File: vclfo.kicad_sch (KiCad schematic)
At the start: 39 parts, among them U10 tl072, U11 tl072, U6 tl072, U7 lm13700, U8 tl072, U9 tl072

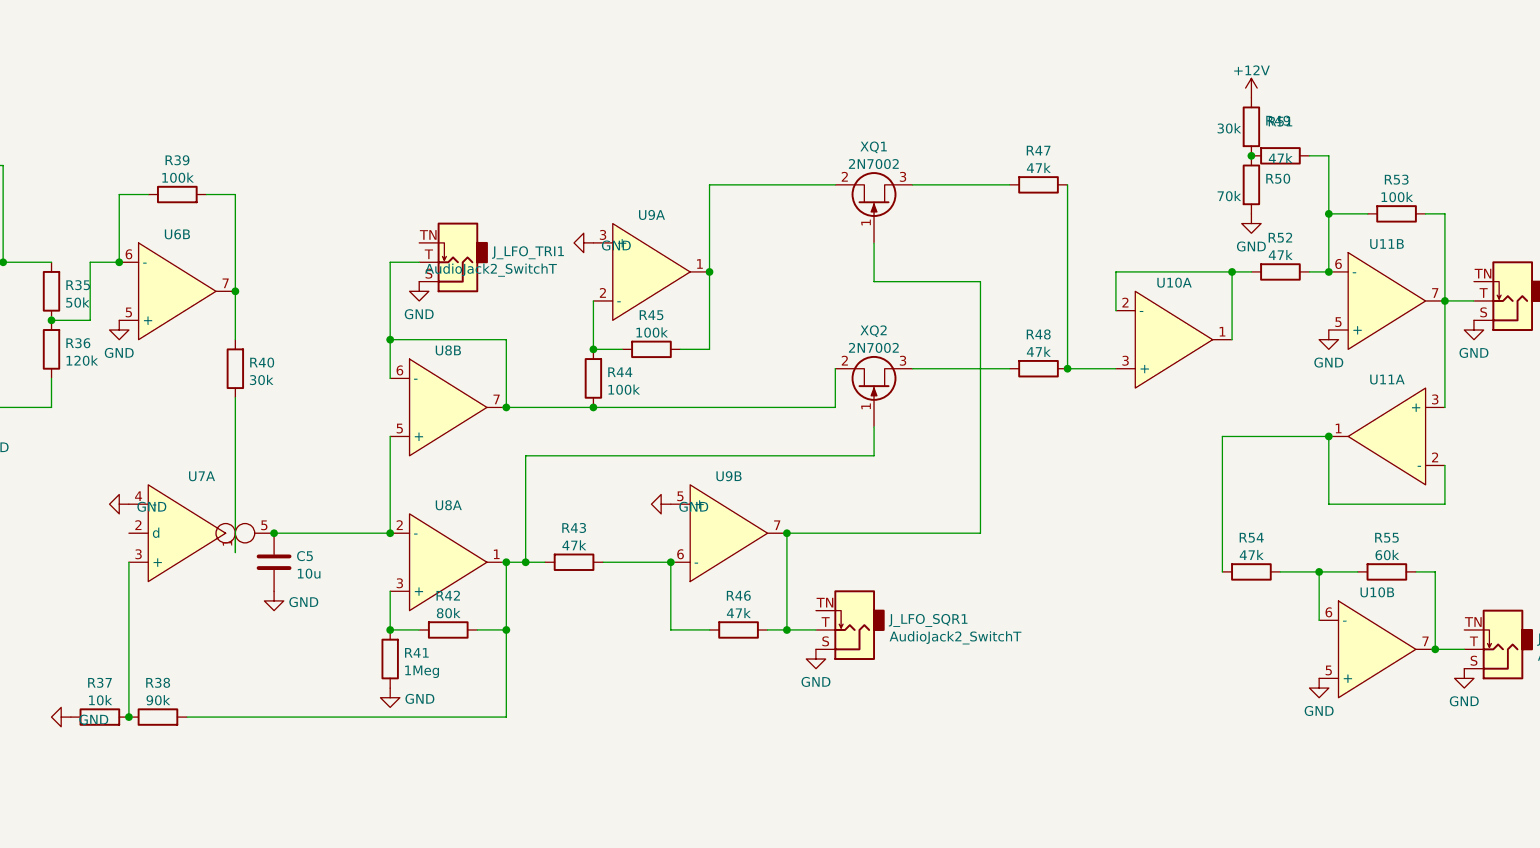
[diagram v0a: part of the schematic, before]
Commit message: adjusted resistor values to standardize and reduce types
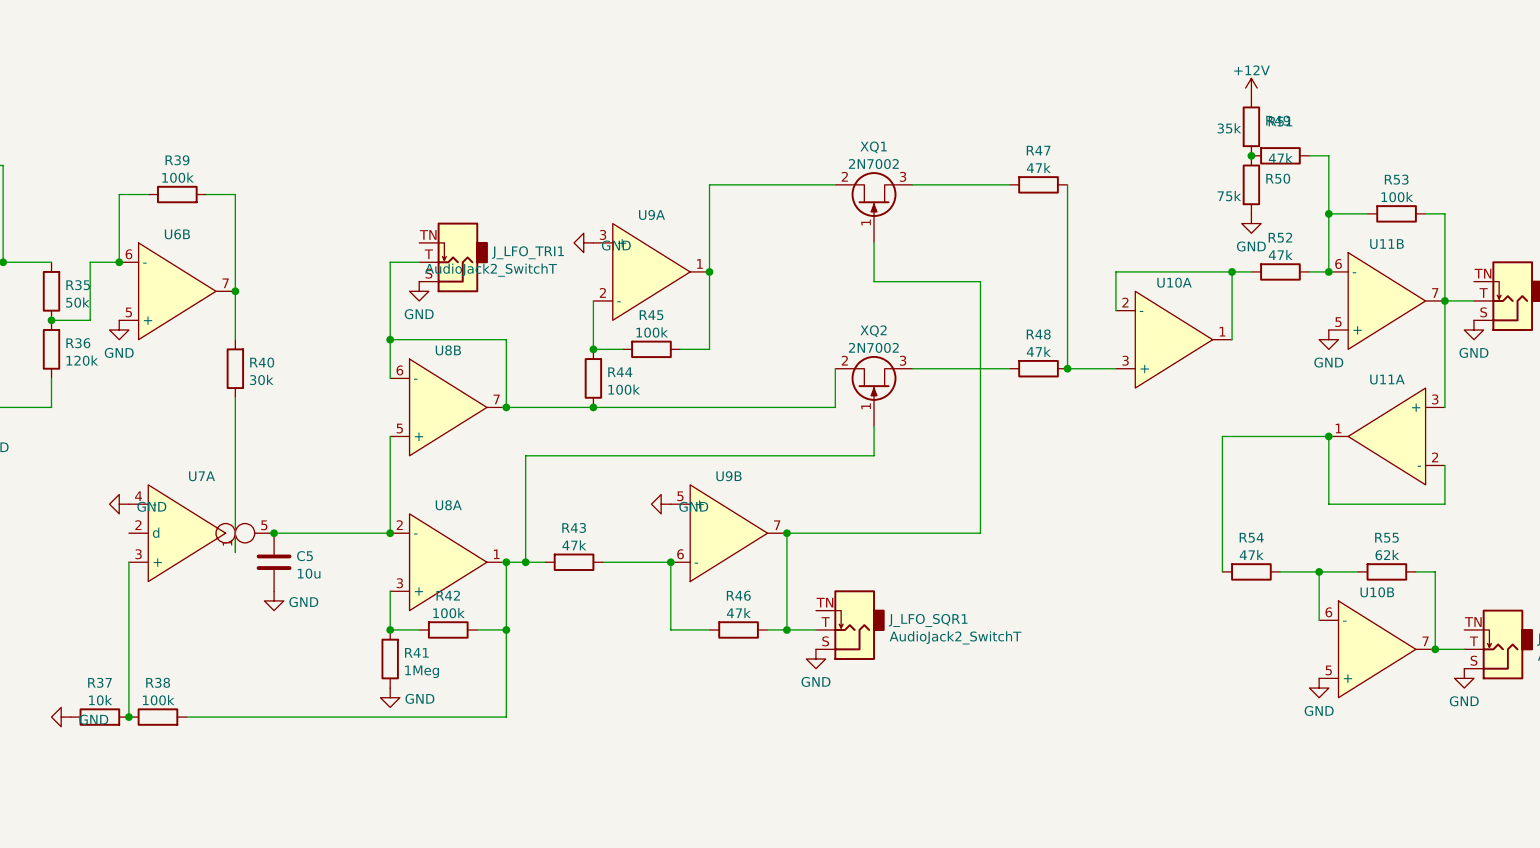
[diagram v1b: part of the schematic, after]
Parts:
- R38: value 90k -> 100k
- R42: value 80k -> 100k
- R49: value 30k -> 35k
- R50: value 70k -> 75k
- R55: value 60k -> 62k
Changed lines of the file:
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@@
     (in_bom yes) (on_board yes) (fields_autoplaced)
     (property "Reference" "R38" (id 0) (at 91.44 118.7408 90))
-    (property "Value" "90k" (id 1) (at 91.44 121.0395 90))
+    (property "Value" "100k" (id 1) (at 91.44 121.0395 90))
     (property "Footprint" "" (id 2) (at 91.44 124.968 90)
       (effects (font (size 1.27 1.27)) hide)
@@
     (in_bom yes) (on_board yes) (fields_autoplaced)
     (property "Reference" "R42" (id 0) (at 129.54 107.3108 90))
-    (property "Value" "80k" (id 1) (at 129.54 109.6095 90))
+    (property "Value" "100k" (id 1) (at 129.54 109.6095 90))
     (property "Footprint" "" (id 2) (at 129.54 109.982 90)
       (effects (font (size 1.27 1.27)) hide)
@@
       (effects (font (size 1.27 1.27)) (justify left))
     )
-    (property "Value" "30k" (id 1) (at 230.3781 45.9878 0)
+    (property "Value" "35k" (id 1) (at 230.3781 45.9878 0)
       (effects (font (size 1.27 1.27)) (justify left))
     )
@@
       (effects (font (size 1.27 1.27)) (justify left))
     )
-    (property "Value" "70k" (id 1) (at 230.3781 54.8778 0)
+    (property "Value" "75k" (id 1) (at 230.3781 54.8778 0)
       (effects (font (size 1.27 1.27)) (justify left))
     )
@@
     (in_bom yes) (on_board yes) (fields_autoplaced)
     (property "Reference" "R55" (id 0) (at 252.73 99.6908 90))
-    (property "Value" "60k" (id 1) (at 252.73 101.9895 90))
+    (property "Value" "62k" (id 1) (at 252.73 101.9895 90))
     (property "Footprint" "" (id 2) (at 252.73 102.362 90)
       (effects (font (size 1.27 1.27)) hide)
